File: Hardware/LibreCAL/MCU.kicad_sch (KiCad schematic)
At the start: 30 parts, among them J5 USB_C_Receptacle_USB2.0, J6 TC2030-ARM, SW1 TL3301NF160QG, U5 W25Q16JVSNIQ, U6 IP4234CZ6, U7 RP2040, U8 W25Q16JVSNIQ, Y1 ECS-120-8-36-CKM-TR3

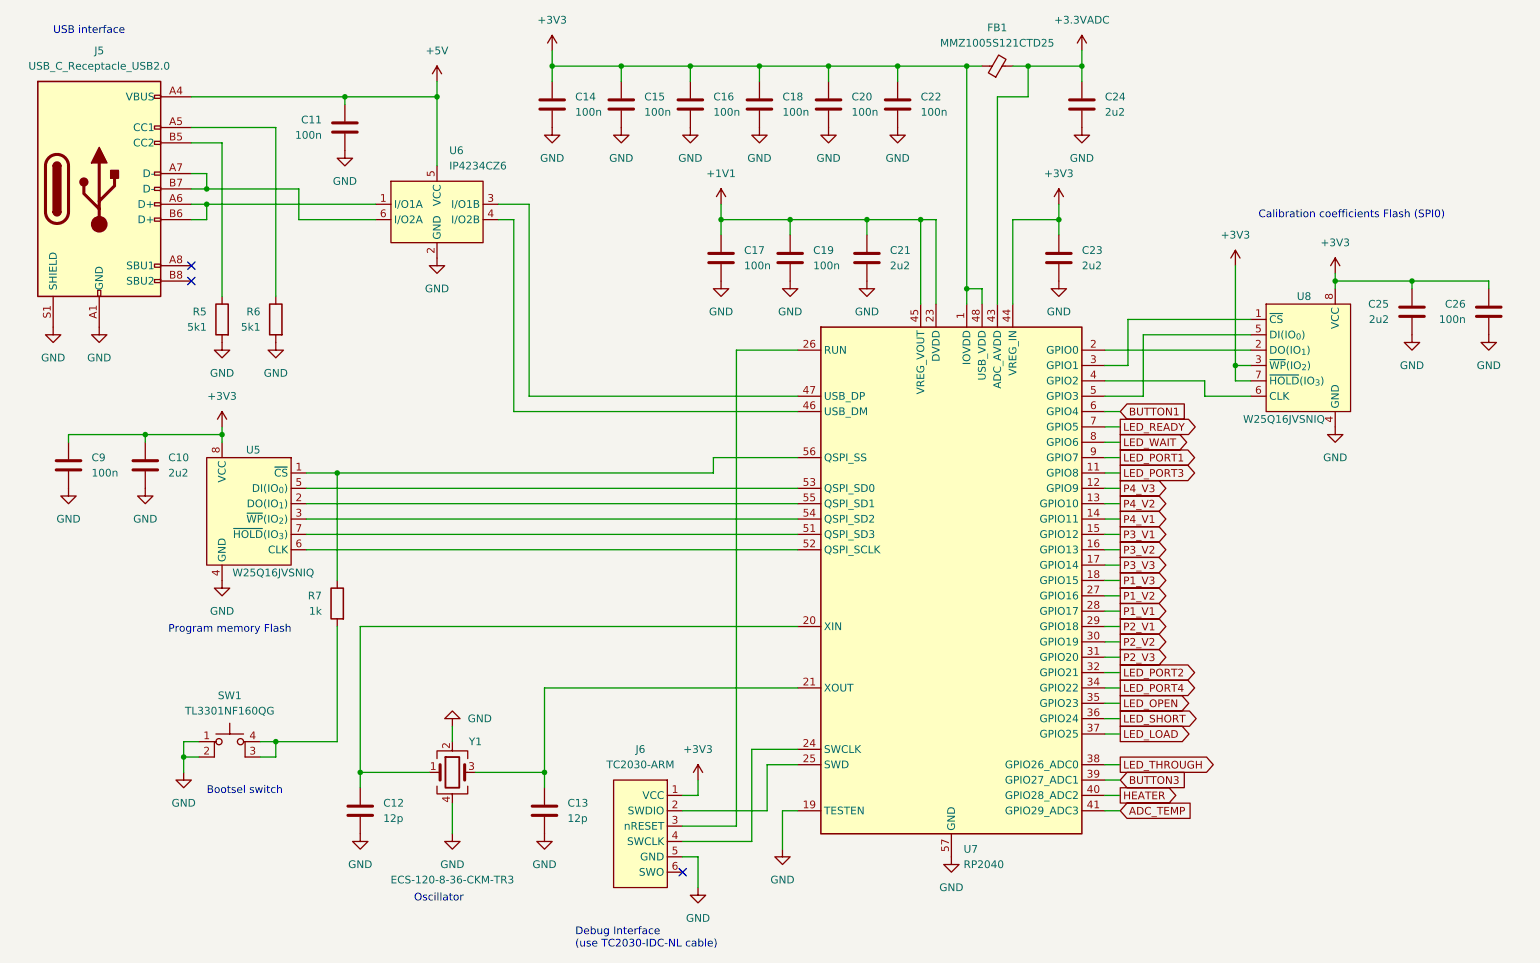
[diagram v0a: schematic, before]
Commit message: update to larger flash for calibration coefficients
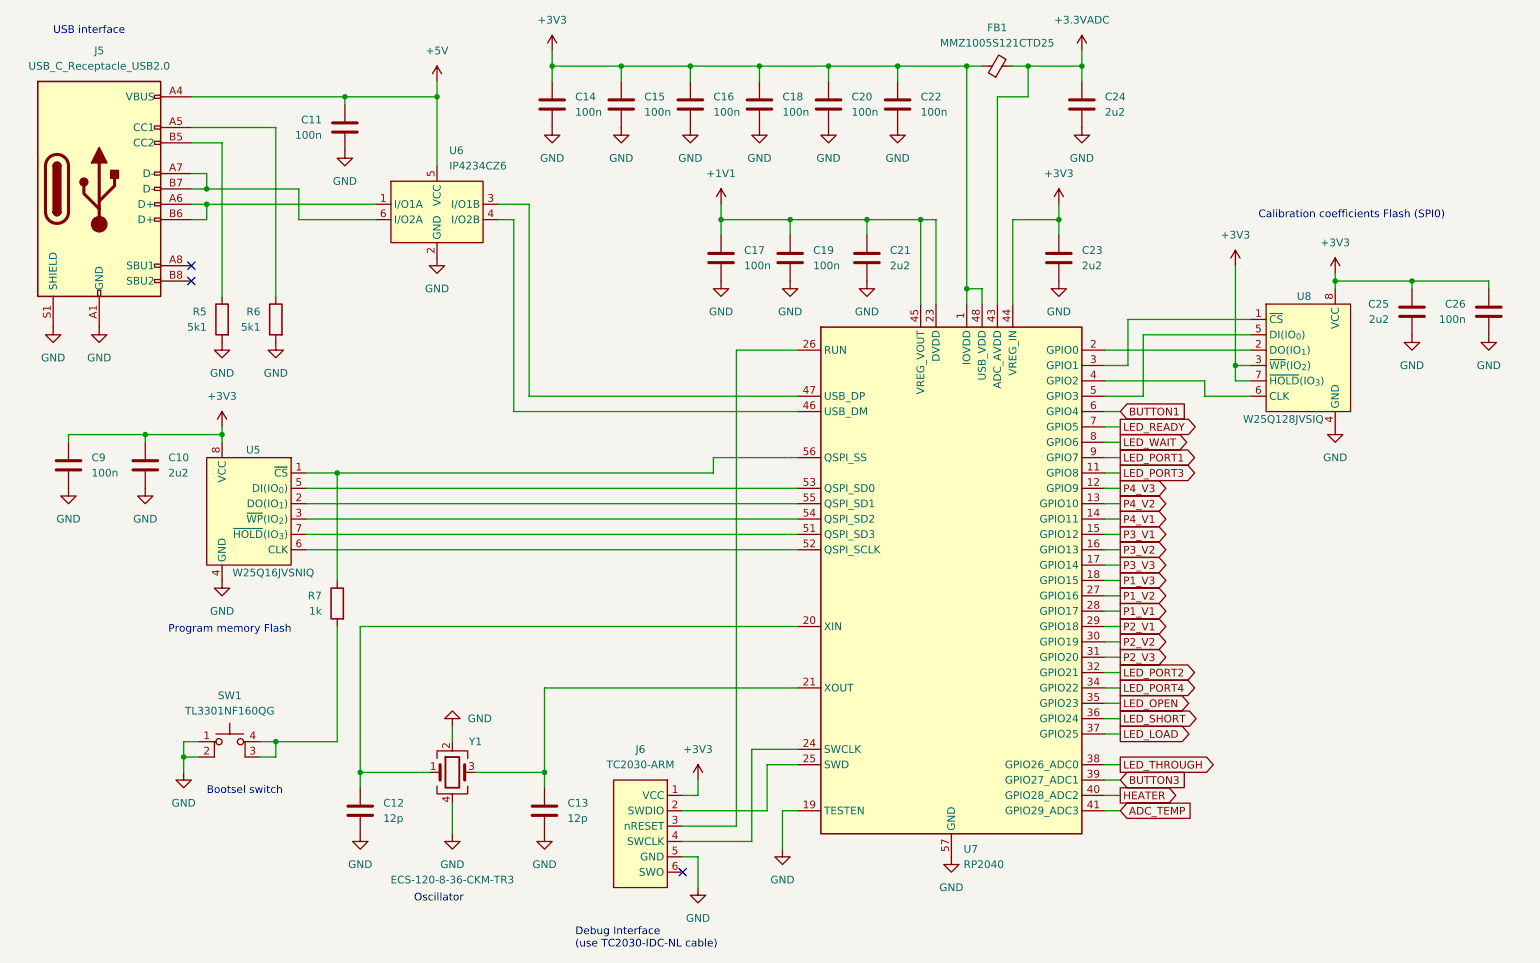
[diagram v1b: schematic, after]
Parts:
- U8: value W25Q16JVSNIQ -> W25Q128JVSIQ; footprint Package_SO:SOIC-8_3.9x4.9mm_P1.27mm -> Package_SO:SOIC-8_5.23x5.23mm_P1.27mm
